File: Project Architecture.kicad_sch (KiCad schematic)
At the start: 0 parts

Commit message: added schematics and pcb, configure project
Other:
- sheet Section A - Title A renamed MCU - Power
- sheet Section B - Title B renamed MCU - IO
- added sheet Interface - RF Transmitter 2.4GHz (Transmitter - 2.4GHz.kicad_sch)
- added sheet Interface - USB (Power and USB.kicad_sch)
- added sheet LCD - Backlight (LCD - Backlight.kicad_sch)
- added sheet LCD - Connectors (LCD.kicad_sch)
- added sheet Memory - EEPROM (Memory - EEPROM.kicad_sch)
- added sheet Memory - Flash (MCU - FLASH.kicad_sch)
- added sheet Memory - SD Card (MCU - SD Card.kicad_sch)
- added sheet Memory - SDRAM (MCU - Memory.kicad_sch)
- added sheet Power - Battery (Battery.kicad_sch)
- added sheet Power - Charging (Power - Charging .kicad_sch)
- added sheet Power - Generation (Power - Generation.kicad_sch)
- added sheet UI - Buttons (Buttons.kicad_sch)
- added sheet UI - Joysticks (Joysticks.kicad_sch)
- added sheet UI - LEDs (UI - LEDs.kicad_sch)
- added sheet UI - Rotary encoders (Rotary encoders.kicad_sch)
- added sheet UI - Toggle switches (Toggle switches.kicad_sch)
- sheet MCU - IO: file Section B - TItle B.kicad_sch -> MCU - IO.kicad_sch
- sheet MCU - IO ports: added {ADC1}, {BACKLIGHT_PWM}, {CTP}, {FMC}, {I2C3}, {LTDC}, {QUADSPI}, {RCC_OSC}, {SDMMC2}, {SPI5}, {SWD}, {TIM2}, {USB_OTG_FS}; removed none
- sheet MCU - Power: file Section A - Title A.kicad_sch -> MCU - Power.kicad_sch

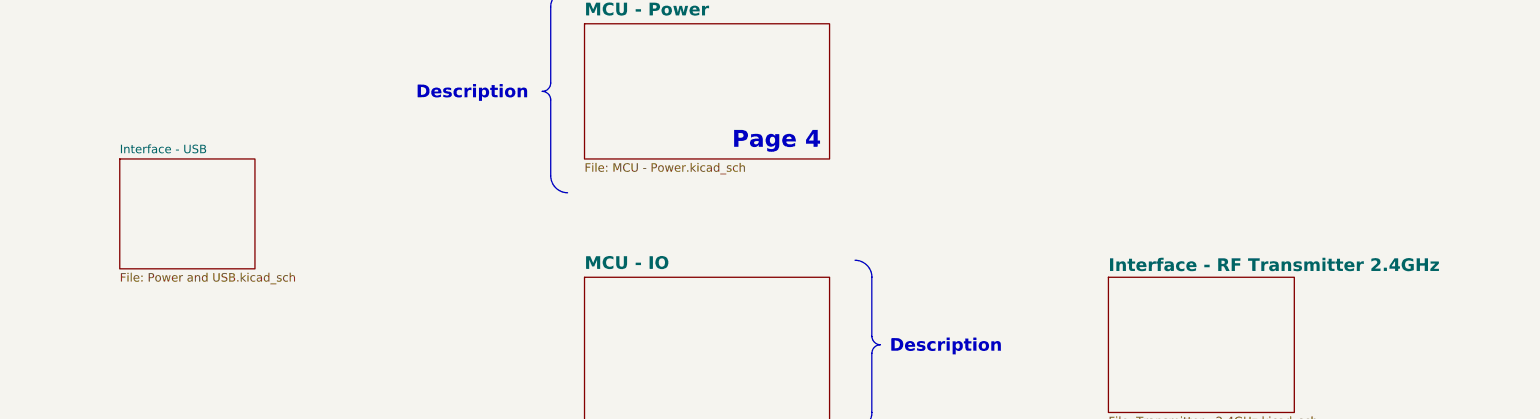
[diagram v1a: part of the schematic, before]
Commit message: added sd card schematic and refactor page numbers and general tab
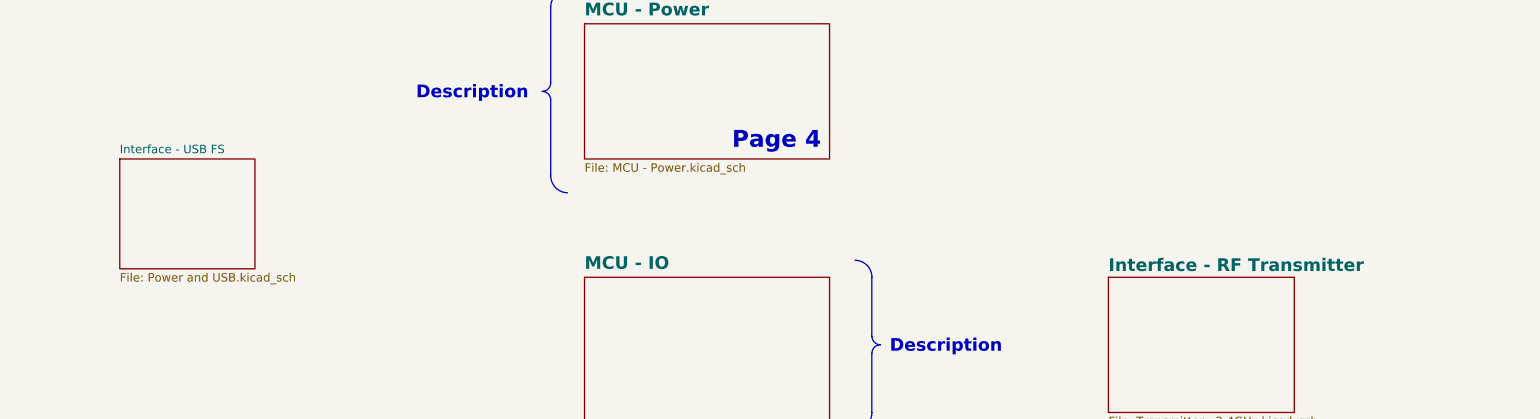
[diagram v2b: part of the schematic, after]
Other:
- sheet Interface - RF Transmitter 2.4GHz renamed Interface - RF Transmitter
- sheet Interface - USB renamed Interface - USB FS
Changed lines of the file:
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@@
 			(project "transmitter"
 				(path "/0650c7a8-acba-429c-9f8e-eec0baf0bc1c/fede4c36-00cc-4d3d-b71c-5243ba232202"
-					(page "14")
+					(page "20")
 				)
 			)
@@
 			(project "transmitter"
 				(path "/0650c7a8-acba-429c-9f8e-eec0baf0bc1c/fede4c36-00cc-4d3d-b71c-5243ba232202"
-					(page "17")
+					(page "5")
 				)
 			)
@@
 			(project "transmitter"
 				(path "/0650c7a8-acba-429c-9f8e-eec0baf0bc1c/fede4c36-00cc-4d3d-b71c-5243ba232202"
-					(page "8")
+					(page "11")
 				)
 			)
@@
 			(project "transmitter"
 				(path "/0650c7a8-acba-429c-9f8e-eec0baf0bc1c/fede4c36-00cc-4d3d-b71c-5243ba232202"
-					(page "10")
+					(page "16")
 				)
 			)
@@
 			(color 0 0 0 0.0000)
 		)
-		(property "Sheetname" "Interface - RF Transmitter 2.4GHz"
+		(property "Sheetname" "Interface - RF Transmitter"
 			(at 279.4 84.3784 0)
 			(effects
@@
 			(project "transmitter"
 				(path "/0650c7a8-acba-429c-9f8e-eec0baf0bc1c/fede4c36-00cc-4d3d-b71c-5243ba232202"
-					(page "8")
+					(page "14")
 				)
 			)
@@
 			(project "transmitter"
 				(path "/0650c7a8-acba-429c-9f8e-eec0baf0bc1c/fede4c36-00cc-4d3d-b71c-5243ba232202"
-					(page "22")
+					(page "10")
 				)
 			)
@@
 			(project "transmitter"
 				(path "/0650c7a8-acba-429c-9f8e-eec0baf0bc1c/fede4c36-00cc-4d3d-b71c-5243ba232202"
-					(page "6")
+					(page "8")
 				)
 			)
@@
 			(project "transmitter"
 				(path "/0650c7a8-acba-429c-9f8e-eec0baf0bc1c/fede4c36-00cc-4d3d-b71c-5243ba232202"
-					(page "19")
+					(page "6")
 				)
 			)
@@
 			(color 0 0 0 0.0000)
 		)
-		(property "Sheetname" "Interface - USB"
+		(property "Sheetname" "Interface - USB FS"
 			(at 130.81 66.5984 0)
 			(effects
@@
 			(project "transmitter"
 				(path "/0650c7a8-acba-429c-9f8e-eec0baf0bc1c/fede4c36-00cc-4d3d-b71c-5243ba232202"
-					(page "5")
+					(page "13")
 				)
 			)
@@
 			(project "transmitter"
 				(path "/0650c7a8-acba-429c-9f8e-eec0baf0bc1c/fede4c36-00cc-4d3d-b71c-5243ba232202"
-					(page "16")
+					(page "17")
 				)
 			)
@@
 			(project "transmitter"
 				(path "/0650c7a8-acba-429c-9f8e-eec0baf0bc1c/fede4c36-00cc-4d3d-b71c-5243ba232202"
-					(page "13")
+					(page "18")
 				)
 			)
@@
 			(project "transmitter"
 				(path "/0650c7a8-acba-429c-9f8e-eec0baf0bc1c/fede4c36-00cc-4d3d-b71c-5243ba232202"
-					(page "18")
+					(page "15")
 				)
 			)
@@
 			(project "transmitter"
 				(path "/0650c7a8-acba-429c-9f8e-eec0baf0bc1c/fede4c36-00cc-4d3d-b71c-5243ba232202"
-					(page "20")
+					(page "7")
 				)
 			)
@@
 			(project "transmitter"
 				(path "/0650c7a8-acba-429c-9f8e-eec0baf0bc1c/fede4c36-00cc-4d3d-b71c-5243ba232202"
-					(page "7")
+					(page "9")
 				)
 			)
@@
 			(project "transmitter"
 				(path "/0650c7a8-acba-429c-9f8e-eec0baf0bc1c/fede4c36-00cc-4d3d-b71c-5243ba232202"
-					(page "15")
-				)
-			)
+					(page "19")
+				)
+			)
